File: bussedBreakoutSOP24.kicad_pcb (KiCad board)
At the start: 2 copper layers, 2.9 x 2.9 mm, 49 parts, among them J1 Conn_01x12_Pin, J10 Conn_01x06_Pin, J11 Conn_01x06_Pin, J12 Conn_01x06_Pin, J13 Conn_01x06_Pin, J14 Conn_01x06_Pin, J15 Conn_01x06_Pin, J16 Conn_01x06_Pin, J17 Conn_01x06_Pin, J18 Conn_01x06_Pin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

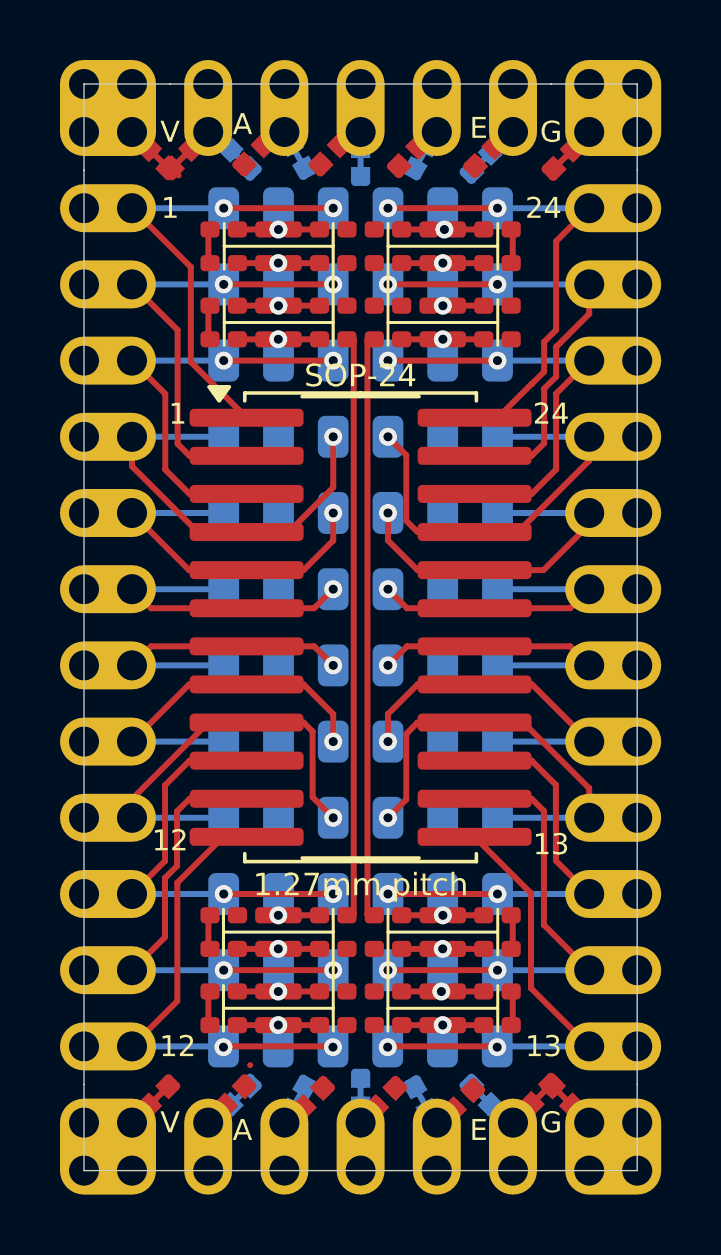
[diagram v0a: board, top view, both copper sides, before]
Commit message: Fix/exclude DRC errors
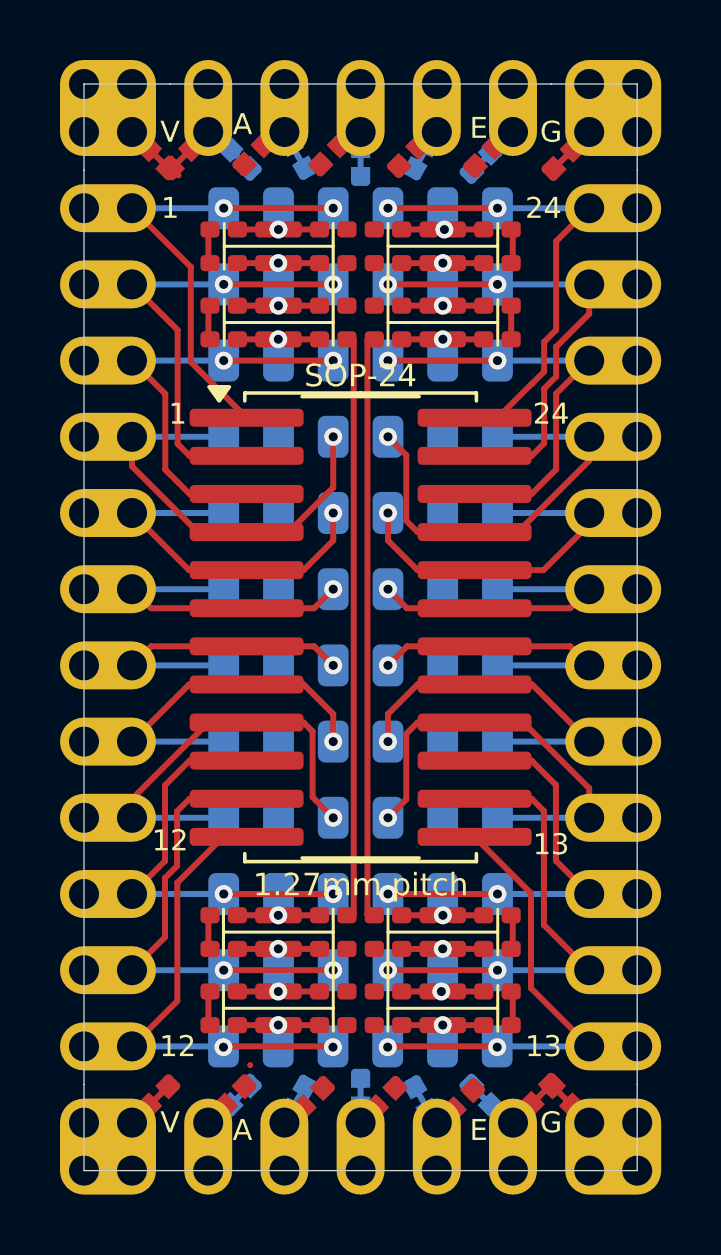
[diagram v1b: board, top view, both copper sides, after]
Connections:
- J4 pad 1: Net-(J4-Pin_1) -> /ET
- J4 pad 2: Net-(J4-Pin_2) -> /DT
- J4 pad 3: Net-(J4-Pin_3) -> /CT
- J4 pad 4: Net-(J4-Pin_4) -> /BT
- J4 pad 5: Net-(J4-Pin_5) -> /AT
- J5 pad 1: Net-(J5-Pin_1) -> /AB
- J5 pad 2: Net-(J5-Pin_2) -> /BB
- J5 pad 3: Net-(J5-Pin_3) -> /CB
- J5 pad 4: Net-(J5-Pin_4) -> /DB
- J5 pad 5: Net-(J5-Pin_5) -> /EB
- JP10 pad 1: Net-(J5-Pin_4) -> /DB
- JP11 pad 2: Net-(J4-Pin_1) -> /ET
- JP12 pad 1: Net-(J5-Pin_5) -> /EB
- JP15 pad 2: /A -> /AT
- JP16 pad 2: /B -> /BT
- JP17 pad 2: /C -> /CT
- JP18 pad 2: /D -> /DT
- JP19 pad 2: /E -> /ET
- JP20 pad 2: /A -> /AB
- JP21 pad 2: /B -> /BB
- JP22 pad 2: /C -> /CB
- JP23 pad 2: /D -> /DB
- JP24 pad 2: /E -> /EB
- JP3 pad 2: Net-(J4-Pin_5) -> /AT
- JP4 pad 1: Net-(J5-Pin_1) -> /AB
- JP5 pad 2: Net-(J4-Pin_4) -> /BT
- JP6 pad 1: Net-(J5-Pin_2) -> /BB
- JP7 pad 2: Net-(J4-Pin_3) -> /CT
- JP8 pad 1: Net-(J5-Pin_3) -> /CB
- JP9 pad 2: Net-(J4-Pin_2) -> /DT
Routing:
- net /10T: track 1.31 -> 3.24 mm
- net /23T: track 2.93 -> 4.86 mm
- net Net-(J23-Pin_23): track 0.00 -> 1.12 mm
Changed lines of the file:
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@@
 	(net 1 "VCC")
 	(net 2 "Net-(J2-Pin_1)")
-	(net 3 "Net-(J5-Pin_3)")
-	(net 4 "Net-(J5-Pin_5)")
+	(net 3 "/AT")
+	(net 4 "/BT")
 	(net 5 "Net-(J3-Pin_1)")
-	(net 6 "Net-(J5-Pin_4)")
-	(net 7 "Net-(J5-Pin_2)")
-	(net 8 "Net-(J4-Pin_3)")
-	(net 9 "Net-(J4-Pin_5)")
-	(net 10 "Net-(J4-Pin_4)")
-	(net 11 "Net-(J4-Pin_2)")
-	(net 12 "Net-(J4-Pin_1)")
-	(net 13 "Net-(J5-Pin_1)")
+	(net 6 "/ET")
+	(net 7 "/CT")
+	(net 8 "/DT")
+	(net 9 "/CB")
+	(net 10 "/EB")
+	(net 11 "/DB")
+	(net 12 "/BB")
+	(net 13 "/AB")
 	(net 14 "GND")
 	(net 15 "/8")
@@
 			(size 0.63 0.37)
 			(layers "F.Cu" "F.Mask")
-			(net 44 "/D")
+			(net 11 "/DB")
 			(pinfunction "B")
 			(pintype "passive")
@@
 			(size 0.63 0.37)
 			(layers "F.Cu" "F.Mask")
-			(net 43 "/C")
+			(net 9 "/CB")
 			(pinfunction "B")
 			(pintype "passive")
@@
 			(size 0.63 0.37)
 			(layers "F.Cu" "F.Mask")
-			(net 45 "/E")
+			(net 10 "/EB")
 			(pinfunction "B")
 			(pintype "passive")
@@
 			(size 0.63 0.37)
 			(layers "F.Cu" "F.Mask")
-			(net 44 "/D")
+			(net 8 "/DT")
 			(pinfunction "B")
 			(pintype "passive")
@@
 			(size 0.63 0.37)
 			(layers "F.Cu" "F.Mask")
-			(net 41 "/A")
+			(net 3 "/AT")
 			(pinfunction "B")
 			(pintype "passive")
@@
 			(size 0.63 0.37)
 			(layers "F.Cu" "F.Mask")
-			(net 42 "/B")
+			(net 12 "/BB")
 			(pinfunction "B")
 			(pintype "passive")
@@
 			(size 0.63 0.37)
 			(layers "F.Cu" "F.Mask")
-			(net 41 "/A")
+			(net 13 "/AB")
 			(pinfunction "B")
 			(pintype "passive")
@@
 			(size 0.63 0.37)
 			(layers "F.Cu" "F.Mask")
-			(net 45 "/E")
+			(net 6 "/ET")
 			(pinfunction "B")
 			(pintype "passive")
@@
 			(size 0.63 0.37)
 			(layers "F.Cu" "F.Mask")
-			(net 42 "/B")
+			(net 4 "/BT")
 			(pinfunction "B")
 			(pintype "passive")
@@
 			(size 0.63 0.37)
 			(layers "F.Cu" "F.Mask")
-			(net 43 "/C")
+			(net 7 "/CT")
 			(pinfunction "B")
 			(pintype "passive")
@@
 			(size 0.63 0.37)
 			(layers "B.Cu" "B.Mask")
-			(net 6 "Net-(J5-Pin_4)")
+			(net 11 "/DB")
 			(pinfunction "A")
 			(pintype "passive")
@@
 			(size 0.63 0.37)
 			(layers "B.Cu" "B.Mask")
-			(net 13 "Net-(J5-Pin_1)")
+			(net 13 "/AB")
 			(pinfunction "A")
 			(pintype "passive")
@@
 			(size 0.63 0.37)
 			(layers "B.Cu" "B.Mask")
-			(net 10 "Net-(J4-Pin_4)")
+			(net 4 "/BT")
 			(pinfunction "B")
 			(pintype "passive")
@@
 			(size 0.63 0.37)
 			(layers "B.Cu" "B.Mask")
-			(net 11 "Net-(J4-Pin_2)")
+			(net 8 "/DT")
 			(pinfunction "B")
 			(pintype "passive")
@@
 			(remove_unused_layers no)
 			(roundrect_rratio 0.5)
-			(net 13 "Net-(J5-Pin_1)")
+			(net 13 "/AB")
 			(pinfunction "Pin_1")
 			(pintype "passive")
@@
 			(remove_unused_layers no)
 			(roundrect_rratio 0.5)
-			(net 13 "Net-(J5-Pin_1)")
+			(net 13 "/AB")
 			(pinfunction "Pin_1")
 			(pintype "passive")
@@
 			(remove_unused_layers no)
 			(roundrect_rratio 0.5)
-			(net 7 "Net-(J5-Pin_2)")
+			(net 12 "/BB")
 			(pinfunction "Pin_2")
 			(pintype "passive")
@@
 			(remove_unused_layers no)
 			(roundrect_rratio 0.5)
-			(net 7 "Net-(J5-Pin_2)")
+			(net 12 "/BB")
 			(pinfunction "Pin_2")
 			(pintype "passive")
@@
 			(remove_unused_layers no)
 			(roundrect_rratio 0.5)
-			(net 3 "Net-(J5-Pin_3)")
+			(net 9 "/CB")
 			(pinfunction "Pin_3")
 			(pintype "passive")
@@
 			(remove_unused_layers no)
 			(roundrect_rratio 0.5)
-			(net 3 "Net-(J5-Pin_3)")
+			(net 9 "/CB")
 			(pinfunction "Pin_3")
 			(pintype "passive")
@@
 			(remove_unused_layers no)
 			(roundrect_rratio 0.5)
-			(net 6 "Net-(J5-Pin_4)")
+			(net 11 "/DB")
 			(pinfunction "Pin_4")
 			(pintype "passive")
@@
 			(remove_unused_layers no)
 			(roundrect_rratio 0.5)
-			(net 6 "Net-(J5-Pin_4)")
+			(net 11 "/DB")
 			(pinfunction "Pin_4")
 			(pintype "passive")
@@
 			(remove_unused_layers no)
 			(roundrect_rratio 0.5)
-			(net 4 "Net-(J5-Pin_5)")
+			(net 10 "/EB")
 			(pinfunction "Pin_5")
 			(pintype "passive")
@@
 			(remove_unused_layers no)
 			(roundrect_rratio 0.5)
-			(net 4 "Net-(J5-Pin_5)")
+			(net 10 "/EB")
 			(pinfunction "Pin_5")
 			(pintype "passive")
@@
 			(size 0.63 0.37)
 			(layers "B.Cu" "B.Mask")
-			(net 7 "Net-(J5-Pin_2)")
+			(net 12 "/BB")
 			(pinfunction "A")
 			(pintype "passive")
@@
 			(size 0.63 0.37)
 			(layers "B.Cu" "B.Mask")
-			(net 8 "Net-(J4-Pin_3)")
+			(net 7 "/CT")
 			(pinfunction "B")
 			(pintype "passive")
@@
 			(size 0.63 0.37)
 			(layers "B.Cu" "B.Mask")
-			(net 3 "Net-(J5-Pin_3)")
+			(net 9 "/CB")
 			(pinfunction "A")
 			(pintype "passive")
@@
 			(size 0.63 0.37)
 			(layers "B.Cu" "B.Mask")
-			(net 9 "Net-(J4-Pin_5)")
+			(net 3 "/AT")
 			(pinfunction "B")
 			(pintype "passive")
@@
 			(size 0.63 0.37)
 			(layers "B.Cu" "B.Mask")
-			(net 4 "Net-(J5-Pin_5)")
+			(net 10 "/EB")
 			(pinfunction "A")
 			(pintype "passive")
@@
 			(remove_unused_layers no)
 			(roundrect_rratio 0.5)
-			(net 12 "Net-(J4-Pin_1)")
+			(net 6 "/ET")
 			(pinfunction "Pin_1")
 			(pintype "passive")
@@
 			(remove_unused_layers no)
 			(roundrect_rratio 0.5)
-			(net 12 "Net-(J4-Pin_1)")
+			(net 6 "/ET")
 			(pinfunction "Pin_1")
 			(pintype "passive")
@@
 			(remove_unused_layers no)
 			(roundrect_rratio 0.5)
-			(net 11 "Net-(J4-Pin_2)")
+			(net 8 "/DT")
 			(pinfunction "Pin_2")
 			(pintype "passive")
@@
 			(remove_unused_layers no)
 			(roundrect_rratio 0.5)
-			(net 11 "Net-(J4-Pin_2)")
+			(net 8 "/DT")
 			(pinfunction "Pin_2")
 			(pintype "passive")
@@
 			(remove_unused_layers no)
 			(roundrect_rratio 0.5)
-			(net 8 "Net-(J4-Pin_3)")
+			(net 7 "/CT")
 			(pinfunction "Pin_3")
 			(pintype "passive")
@@
 			(remove_unused_layers no)
 			(roundrect_rratio 0.5)
-			(net 8 "Net-(J4-Pin_3)")
+			(net 7 "/CT")
 			(pinfunction "Pin_3")
 			(pintype "passive")
@@
 			(remove_unused_layers no)
 			(roundrect_rratio 0.5)
-			(net 10 "Net-(J4-Pin_4)")
+			(net 4 "/BT")
 			(pinfunction "Pin_4")
 			(pintype "passive")
@@
 			(remove_unused_layers no)
 			(roundrect_rratio 0.5)
-			(net 10 "Net-(J4-Pin_4)")
+			(net 4 "/BT")
 			(pinfunction "Pin_4")
 			(pintype "passive")
@@
 			(remove_unused_layers no)
 			(roundrect_rratio 0.5)
-			(net 9 "Net-(J4-Pin_5)")
+			(net 3 "/AT")
 			(pinfunction "Pin_5")
 			(pintype "passive")
@@
 			(remove_unused_layers no)
 			(roundrect_rratio 0.5)
-			(net 9 "Net-(J4-Pin_5)")
+			(net 3 "/AT")
 			(pinfunction "Pin_5")
 			(pintype "passive")
@@
 			(size 0.63 0.37)
 			(layers "B.Cu" "B.Mask")
-			(net 12 "Net-(J4-Pin_1)")
+			(net 6 "/ET")
 			(pinfunction "B")
 			(pintype "passive")
@@
 	)
 	(segment
-		(start 35.7607 29.7713)
-		(end 35.7632 29.7688)
+		(start 37.12625 31.1887)
+		(end 34.38875 31.1887)
 		(width 0.2)
 		(layer "F.Cu")
@@
 	)
 	(segment
-		(start 36.2675 31.1887)
-		(end 37.0725 31.1887)
+		(start 35.7607 29.7713)
+		(end 35.7632 29.7688)
 		(width 0.2)
 		(layer "F.Cu")
@@
 	)
 	(segment
-		(start 30.2743 51.5087)
-		(end 30.2768 51.5112)
+		(start 31.65125 51.5087)
+		(end 28.91375 51.5087)
 		(width 0.2)
 		(layer "F.Cu")
@@
 	)
 	(segment
-		(start 30.7925 51.5087)
-		(end 31.5975 51.5087)
+		(start 30.2743 51.5087)
+		(end 30.2768 51.5112)
 		(width 0.2)
 		(layer "F.Cu")
@@
 	)
 	(segment
+		(start 38.03875 32.3113)
+		(end 38.03875 31.1887)
+		(width 0.2)
+		(layer "F.Cu")
+		(net 73)
+	)
+	(segment
